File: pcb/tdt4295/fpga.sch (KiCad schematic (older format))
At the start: 47 parts, among them J301 FPGA__debug, U301 S25FL127SABMFV101, U302 NUP4114UCW1T2G, U303 XC7A100T-FTG256-tdt4295

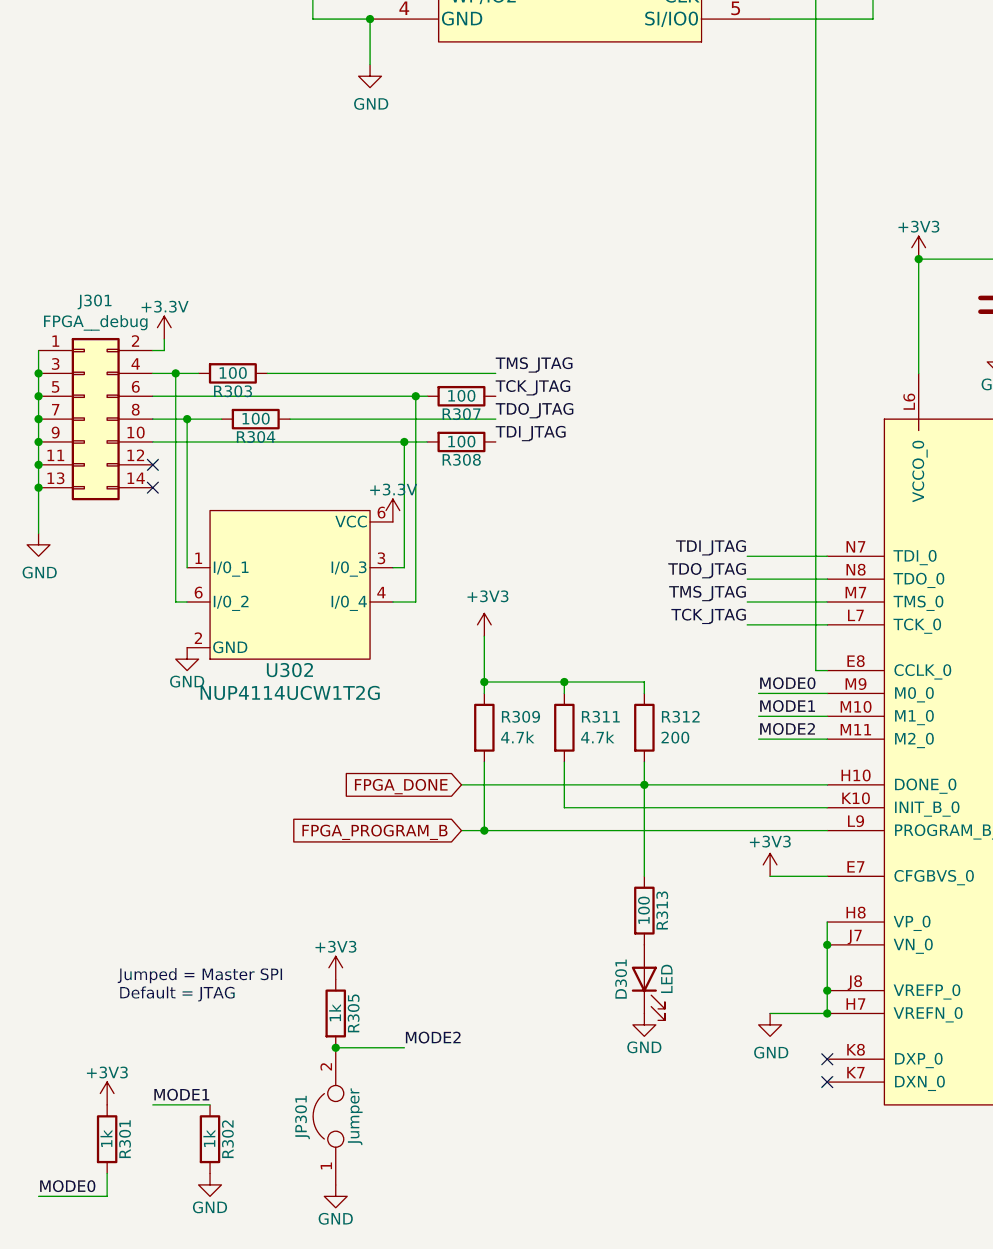
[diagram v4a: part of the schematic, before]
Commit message: remove jumper, add pull-ups for JTAG
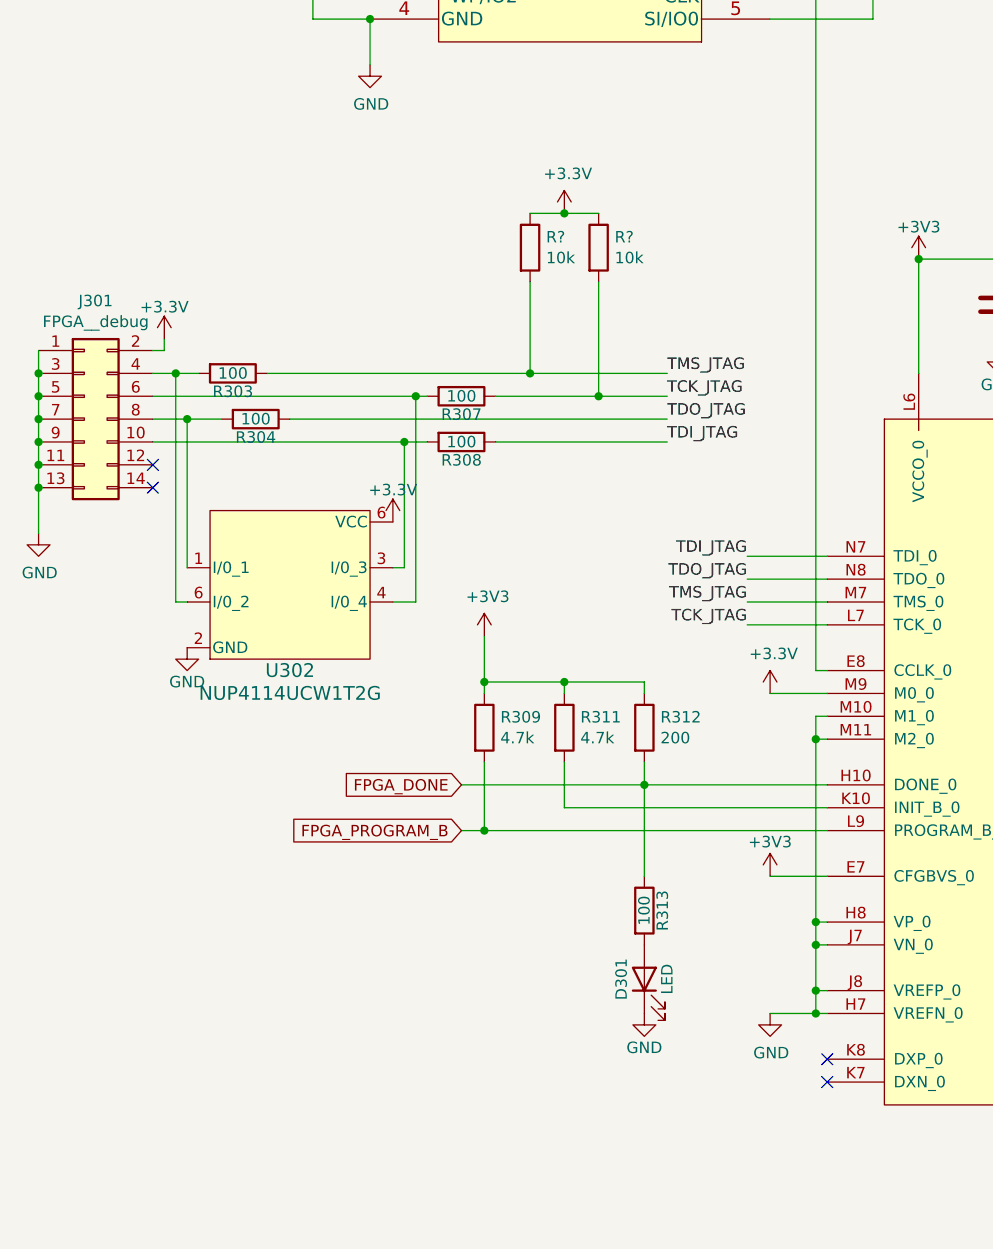
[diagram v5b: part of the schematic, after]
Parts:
- removed JP301: Jumper, Connector_PinSocket_2.54mm:PinSocket_1x02_P2.54mm_Vertical, symbol Device:Jumper
- removed R301, R302, R305: 1k, Resistor_SMD:R_0805_2012Metric_Pad1.20x1.40mm_HandSolder, symbol Device:R
- added R? (x2): 10k, symbol Device:R
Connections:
- net MODE0 is gone; now on net +3V3: U303.M9 (M0_0)
- net MODE1 is gone; now on net GND: U303.M10 (M1_0)
- net MODE2 is gone; now on net GND: U303.M11 (M2_0)
- net +3V3: now also R?.1, R?.1
- net TCK_JTAG: now also R?.2
- net TMS_JTAG: now also R?.2
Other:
- note removed: "Jumped = Master SPI\nDefault = JTAG"
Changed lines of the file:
@@
 	1    0    0    -1
 $EndComp
-Connection ~ 4000 6850
-Wire Wire Line
-	3750 6850 4000 6850
-Wire Wire Line
-	4000 6750 4000 6850
-Connection ~ 4000 6750
-Wire Wire Line
-	4000 6550 4000 6750
-Connection ~ 4000 6550
-Wire Wire Line
-	4000 6450 4000 6550
+Wire Wire Line
+	3750 6850 3950 6850
 Wire Wire Line
 	2000 1750 2300 1750
@@
 	1    0    0    -1
 $EndComp
-Text Label 2150 7000 0    50   ~ 0
-MODE2
 Wire Wire Line
 	3750 6250 4000 6250
-Wire Wire Line
-	4000 5450 3700 5450
-Wire Wire Line
-	4000 5550 3700 5550
-Wire Wire Line
-	4000 5650 3700 5650
-Text Label 3700 5450 0    50   ~ 0
-MODE0
-Text Label 3700 5550 0    50   ~ 0
-MODE1
-Text Label 3700 5650 0    50   ~ 0
-MODE2
-$Comp
-L power:GND #PWR0307
-U 1 1 618E8B3B
-P 1850 7600
-F 0 "#PWR0307" H 1850 7350 50  0001 C CNN
-F 1 "GND" H 1850 7450 50  0000 C CNN
-F 2 "" H 1850 7600 50  0001 C CNN
-F 3 "" H 1850 7600 50  0001 C CNN
-	1    1850 7600
-	1    0    0    -1
-$EndComp
-$Comp
-L Device:R R305
-U 1 1 618E96EF
-P 1850 6850
-F 0 "R305" V 1930 6850 50  0000 C CNN
-F 1 "1k" V 1850 6850 50  0000 C CNN
-F 2 "Resistor_SMD:R_0805_2012Metric_Pad1.20x1.40mm_HandSolder" V 1780 6850 50  0001 C CNN
-F 3 "https://www.susumu.co.jp/common/pdf/n_catalog_partition05_en.pdf" H 1850 6850 50  0001 C CNN
-F 4 "RR0510P-102-D" H 1850 6850 50  0001 C CNN "Component name"
-F 5 "https://www.digikey.no/product-detail/en/susumu/RR1220P-102-D/RR12P1-0KDCT-ND/432830" H 1850 6850 50  0001 C CNN "DK_Detail_Page"
-	1    1850 6850
-	1    0    0    -1
-$EndComp
-$Comp
-L power:+3V3 #PWR0306
-U 1 1 618EA756
-P 1850 6700
-F 0 "#PWR0306" H 1850 6550 50  0001 C CNN
-F 1 "+3V3" H 1850 6840 50  0000 C CNN
-F 2 "" H 1850 6700 50  0001 C CNN
-F 3 "" H 1850 6700 50  0001 C CNN
-	1    1850 6700
-	1    0    0    -1
-$EndComp
-$Comp
-L Device:R R302
-U 1 1 619371E0
-P 1300 7400
-F 0 "R302" V 1380 7400 50  0000 C CNN
-F 1 "1k" V 1300 7400 50  0000 C CNN
-F 2 "Resistor_SMD:R_0805_2012Metric_Pad1.20x1.40mm_HandSolder" V 1230 7400 50  0001 C CNN
-F 3 "https://www.susumu.co.jp/common/pdf/n_catalog_partition05_en.pdf" H 1300 7400 50  0001 C CNN
-F 4 "RR0510P-102-D" H 1300 7400 50  0001 C CNN "Component name"
-F 5 "https://www.digikey.no/product-detail/en/susumu/RR1220P-102-D/RR12P1-0KDCT-ND/432830" H 1300 7400 50  0001 C CNN "DK_Detail_Page"
-	1    1300 7400
-	1    0    0    -1
-$EndComp
-$Comp
-L Device:R R301
-U 1 1 61937C9D
-P 850 7400
-F 0 "R301" V 930 7400 50  0000 C CNN
-F 1 "1k" V 850 7400 50  0000 C CNN
-F 2 "Resistor_SMD:R_0805_2012Metric_Pad1.20x1.40mm_HandSolder" V 780 7400 50  0001 C CNN
-F 3 "https://www.susumu.co.jp/common/pdf/n_catalog_partition05_en.pdf" H 850 7400 50  0001 C CNN
-F 4 "RR0510P-102-D" H 850 7400 50  0001 C CNN "Component name"
-F 5 "https://www.digikey.no/product-detail/en/susumu/RR1220P-102-D/RR12P1-0KDCT-ND/432830" H 850 7400 50  0001 C CNN "DK_Detail_Page"
-	1    850  7400
-	1    0    0    -1
-$EndComp
-Wire Wire Line
-	1300 7250 1050 7250
-$Comp
-L power:GND #PWR0305
-U 1 1 6195618C
-P 1300 7550
-F 0 "#PWR0305" H 1300 7300 50  0001 C CNN
-F 1 "GND" H 1300 7400 50  0000 C CNN
-F 2 "" H 1300 7550 50  0001 C CNN
-F 3 "" H 1300 7550 50  0001 C CNN
-	1    1300 7550
-	1    0    0    -1
-$EndComp
-Text Label 1050 7250 0    50   ~ 0
-MODE1
-Text Label 550  7650 0    50   ~ 0
-MODE0
-$Comp
-L power:+3V3 #PWR0302
-U 1 1 619680CF
-P 850 7250
-F 0 "#PWR0302" H 850 7100 50  0001 C CNN
-F 1 "+3V3" H 850 7390 50  0000 C CNN
-F 2 "" H 850 7250 50  0001 C CNN
-F 3 "" H 850 7250 50  0001 C CNN
-	1    850  7250
-	1    0    0    -1
-$EndComp
-Wire Wire Line
-	850  7650 850  7550
-Wire Wire Line
-	550  7650 850  7650
-Text Notes 900  6800 0    50   ~ 0
-Jumped = Master SPI\nDefault = JTAG
-$Comp
-L Device:Jumper JP301
-U 1 1 614EDD7D
-P 1850 7300
-F 0 "JP301" H 1850 7450 50  0000 C CNN
-F 1 "Jumper" H 1850 7220 50  0000 C CNN
-F 2 "Connector_PinSocket_2.54mm:PinSocket_1x02_P2.54mm_Vertical" H 1850 7300 50  0001 C CNN
-F 3 "~" H 1850 7300 50  0001 C CNN
-	1    1850 7300
-	0    -1   -1   0
-$EndComp
-Wire Wire Line
-	1850 7000 2150 7000
-Connection ~ 1850 7000
 Wire Wire Line
 	4400 4050 4400 3550
@@
 	0    1    1    0
 $EndComp
-Text Label 2550 4050 0    50   ~ 0
+Text Label 3300 4050 0    50   ~ 0
 TMS_JTAG
-Wire Wire Line
-	1550 4050 2550 4050
-Wire Wire Line
-	1650 4250 2550 4250
-Text Label 2550 4150 0    50   ~ 0
+Text Label 3300 4150 0    50   ~ 0
 TCK_JTAG
-Text Label 2550 4250 0    50   ~ 0
+Text Label 3300 4250 0    50   ~ 0
 TDO_JTAG
-Text Label 2550 4350 0    50   ~ 0
+Text Label 3300 4350 0    50   ~ 0
 TDI_JTAG
 Wire Wire Line
@@
 $EndComp
 Connection ~ 9800 4750
+Wire Wire Line
+	3950 6850 3950 6750
+Wire Wire Line
+	3950 6750 4000 6750
+Connection ~ 3950 6850
+Wire Wire Line
+	3950 6850 4000 6850
+Wire Wire Line
+	3950 6750 3950 6550
+Wire Wire Line
+	3950 6550 4000 6550
+Connection ~ 3950 6750
+Wire Wire Line
+	3950 6550 3950 6450
+Wire Wire Line
+	3950 6450 4000 6450
+Connection ~ 3950 6550
+Wire Wire Line
+	4000 5650 3950 5650
+Connection ~ 3950 6450
+Wire Wire Line
+	4000 5550 3950 5550
+Wire Wire Line
+	3950 5550 3950 5650
+Connection ~ 3950 5650
+Wire Wire Line
+	3950 5650 3950 6450
+$Comp
+L power:+3.3V #PWR?
+U 1 1 615CAF52
+P 3750 5450
+F 0 "#PWR?" H 3750 5300 50  0001 C CNN
+F 1 "+3.3V" H 3765 5623 50  0000 C CNN
+F 2 "" H 3750 5450 50  0001 C CNN
+F 3 "" H 3750 5450 50  0001 C CNN
+	1    3750 5450
+	1    0    0    -1
+$EndComp
+Wire Wire Line
+	3750 5450 4000 5450
+Wire Wire Line
+	1550 4050 2700 4050
+Wire Wire Line
+	2550 4150 3000 4150
+Wire Wire Line
+	1650 4250 3300 4250
+Wire Wire Line
+	2550 4350 3300 4350
+$Comp
+L Device:R R?
+U 1 1 6163D0D9
+P 2700 3500
+F 0 "R?" H 2770 3546 50  0000 L CNN
+F 1 "10k" H 2770 3455 50  0000 L CNN
+F 2 "" V 2630 3500 50  0001 C CNN
+F 3 "~" H 2700 3500 50  0001 C CNN
+	1    2700 3500
+	1    0    0    -1
+$EndComp
+$Comp
+L Device:R R?
+U 1 1 6163D9D1
+P 3000 3500
+F 0 "R?" H 3070 3546 50  0000 L CNN
+F 1 "10k" H 3070 3455 50  0000 L CNN
+F 2 "" V 2930 3500 50  0001 C CNN
+F 3 "~" H 3000 3500 50  0001 C CNN
+	1    3000 3500
+	1    0    0    -1
+$EndComp
+Wire Wire Line
+	3000 3350 2850 3350
+Wire Wire Line
+	2700 3650 2700 4050
+Connection ~ 2700 4050
+Wire Wire Line
+	2700 4050 3300 4050
+Wire Wire Line
+	3000 3650 3000 4150
+Connection ~ 3000 4150
+Wire Wire Line
+	3000 4150 3300 4150
+$Comp
+L power:+3.3V #PWR?
+U 1 1 6166EA7E
+P 2850 3350
+F 0 "#PWR?" H 2850 3200 50  0001 C CNN
+F 1 "+3.3V" H 2865 3523 50  0000 C CNN
+F 2 "" H 2850 3350 50  0001 C CNN
+F 3 "" H 2850 3350 50  0001 C CNN
+	1    2850 3350
+	1    0    0    -1
+$EndComp
+Connection ~ 2850 3350
+Wire Wire Line
+	2850 3350 2700 3350
 $EndSCHEMATC

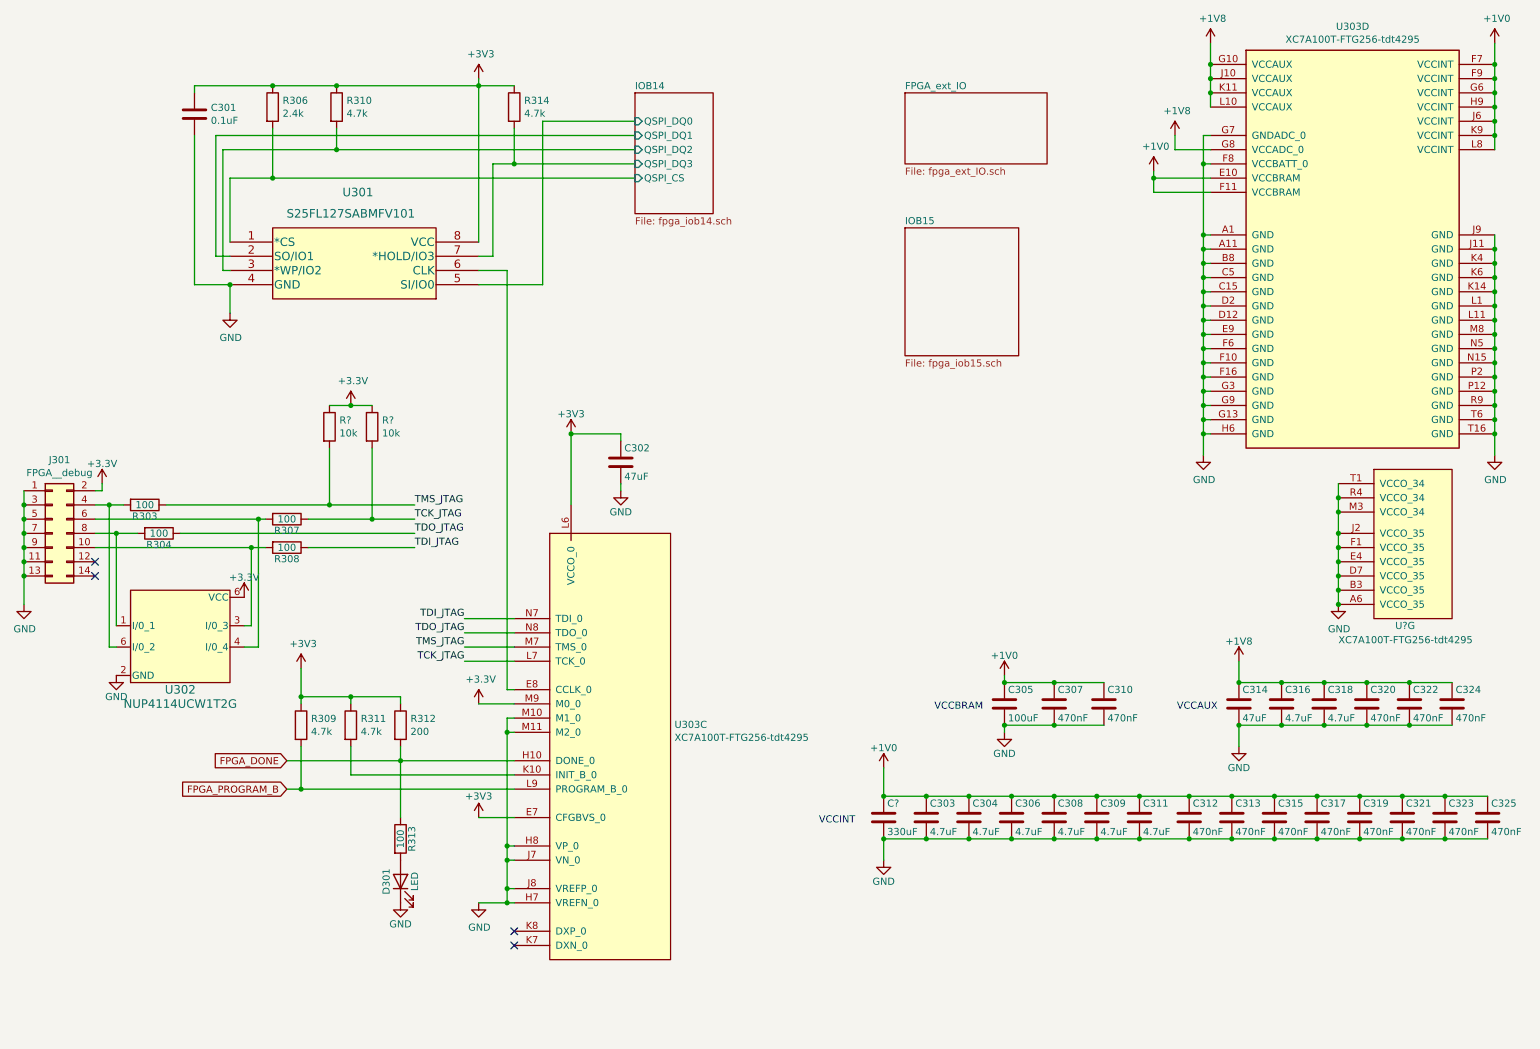
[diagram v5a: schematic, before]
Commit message: add footprints, rename components
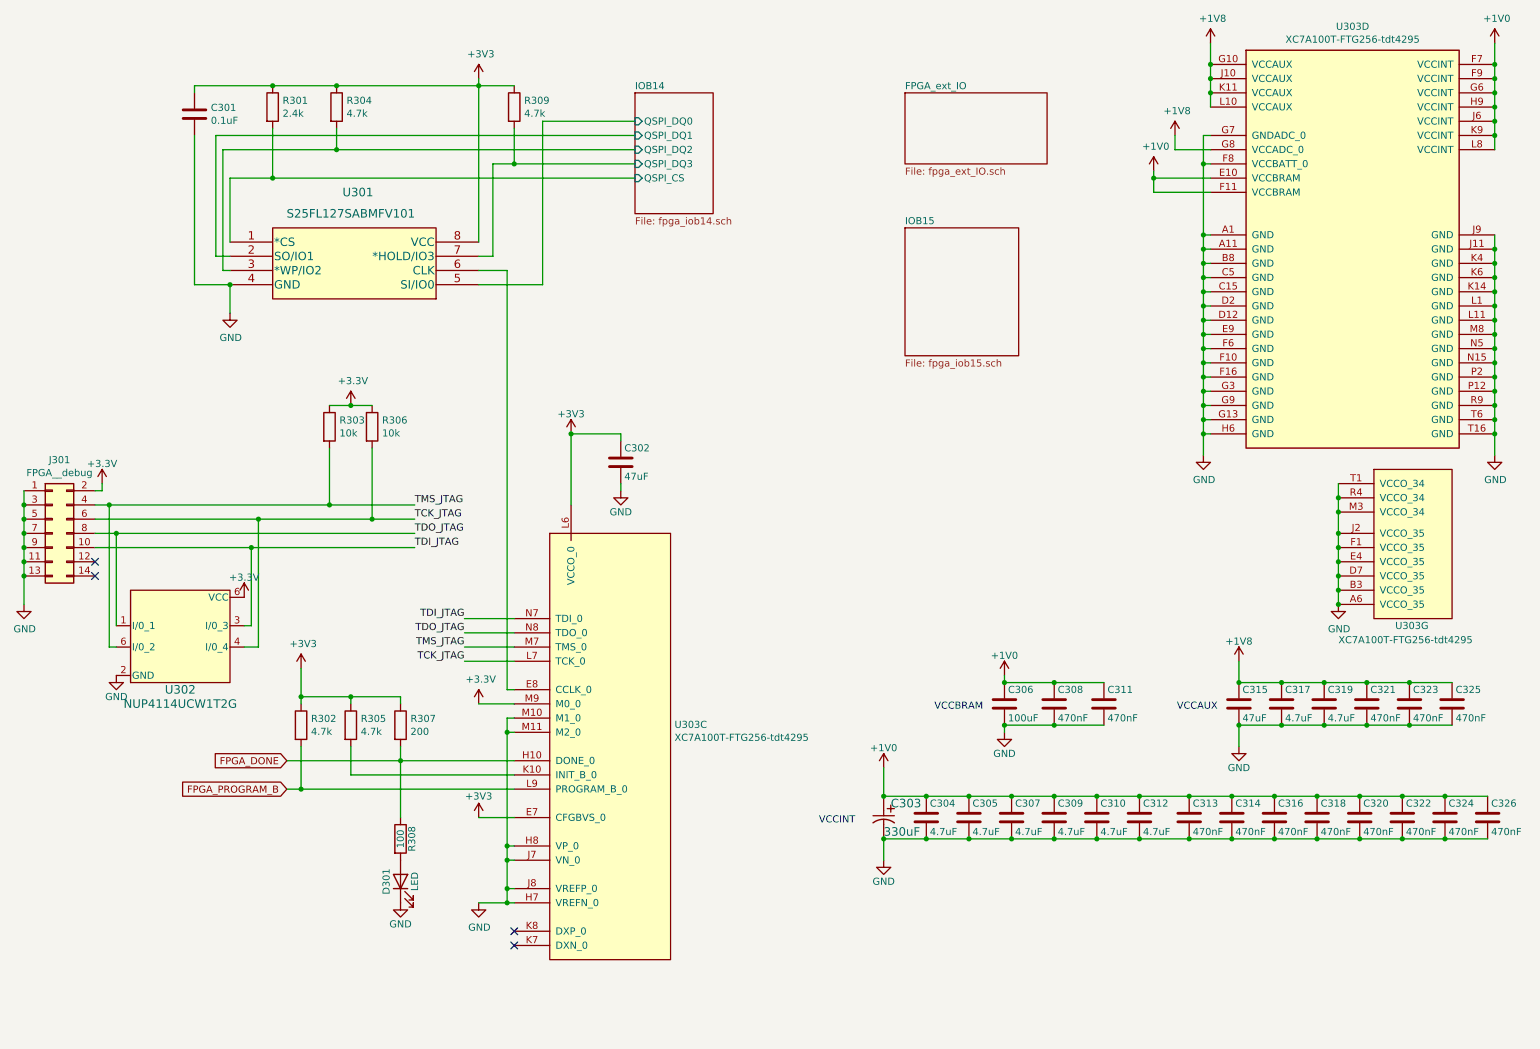
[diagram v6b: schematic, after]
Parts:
- removed C?: 330uF, symbol Device:C
- removed R303, R304, R307, R308: 100, Resistor_SMD:R_0805_2012Metric_Pad1.20x1.40mm_HandSolder, symbol Device:R
- added C303: 330uF, T520V337M2R5ATE025-footprint:T520V337M2R5ATE025, symbol T520V337M2R5ATE025:T520V337M2R5ATE025
- C301: DK_Datasheet_Link (none) -> https://www.digikey.no/product-detail/en/samsung-electro-me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
- C306: renamed from C305; footprint (none) -> Capacitor_SMD:C_1210_3225Metric_Pad1.33x2.70mm_HandSolder; Component name (none) -> CL32A107MPVNNNE; DK_Detail_Page (none) -> https://www.digikey.no/product-detail/en/samsung-electro-me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
- C308: renamed from C307; DK_Detail_Page (none) -> https://www.digikey.no/product-detail/en/murata-electronics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
- C309: renamed from C308; footprint (none) -> Capacitor_SMD:C_0805_2012Metric_Pad1.18x1.45mm_HandSolder; Component name (none) -> C2012X7R1A475K125AC; DK_Detail_Page (none) -> https://www.digikey.no/product-detail/no/tdk-corporation/C2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
- C310: renamed from C309; footprint (none) -> Capacitor_SMD:C_0805_2012Metric_Pad1.18x1.45mm_HandSolder; Component name (none) -> C2012X7R1A475K125AC; DK_Detail_Page (none) -> https://www.digikey.no/product-detail/no/tdk-corporation/C2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
- C311: renamed from C310; DK_Detail_Page (none) -> https://www.digikey.no/product-detail/en/murata-electronics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
- C313: renamed from C312; DK_Detail_Page (none) -> https://www.digikey.no/product-detail/en/murata-electronics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
- C314: renamed from C313; DK_Detail_Page (none) -> https://www.digikey.no/product-detail/en/murata-electronics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
- C316: renamed from C315; DK_Detail_Page (none) -> https://www.digikey.no/product-detail/en/murata-electronics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
- C318: renamed from C317; DK_Detail_Page (none) -> https://www.digikey.no/product-detail/en/murata-electronics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
- C320: renamed from C319; DK_Detail_Page (none) -> https://www.digikey.no/product-detail/en/murata-electronics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
- C321: renamed from C320; DK_Detail_Page (none) -> https://www.digikey.no/product-detail/en/murata-electronics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
- C322: renamed from C321; DK_Detail_Page (none) -> https://www.digikey.no/product-detail/en/murata-electronics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
- C323: renamed from C322; DK_Detail_Page (none) -> https://www.digikey.no/product-detail/en/murata-electronics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
- C324: renamed from C323; DK_Detail_Page (none) -> https://www.digikey.no/product-detail/en/murata-electronics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
- C325: renamed from C324; DK_Detail_Page (none) -> https://www.digikey.no/product-detail/en/murata-electronics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
- C326: renamed from C325; DK_Detail_Page (none) -> https://www.digikey.no/product-detail/en/murata-electronics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
- J301: footprint Connector_PinHeader_2.54mm:PinHeader_1x02_P2.54mm_Vertical -> Connector_PinHeader_2.54mm:PinHeader_2x07_P2.54mm_Vertical
- R303, R306: renamed from R?; footprint (none) -> Resistor_SMD:R_0805_2012Metric_Pad1.20x1.40mm_HandSolder; Component name (none) -> RNCP0805FTD10K0; DK_Detail_Page (none) -> https://www.digikey.no/product-detail/en/stackpole-electron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
- gave numbers to parts that had none: 1
- renumbered C303 to C304, C304 to C305, C306 to C307, C311 to C312, C314 to C315, C316 to C317, C318 to C319, R306 to R301, R309 to R302, R310 to R304, R311 to R305, R312 to R307, R313 to R308, R314 to R309
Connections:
- net +1V0: now also C303.1
- net GND: now also C303.2
- net TCK_JTAG: now also J301.6 (Pin_6), U302.4 (I/0_4)
- net TDI_JTAG: now also J301.10 (Pin_10), U302.3 (I/0_3)
- net TDO_JTAG: now also J301.8 (Pin_8), U302.1 (I/0_1)
- net TMS_JTAG: now also J301.4 (Pin_4), U302.6 (VCC)
